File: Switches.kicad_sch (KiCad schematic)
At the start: 29 parts

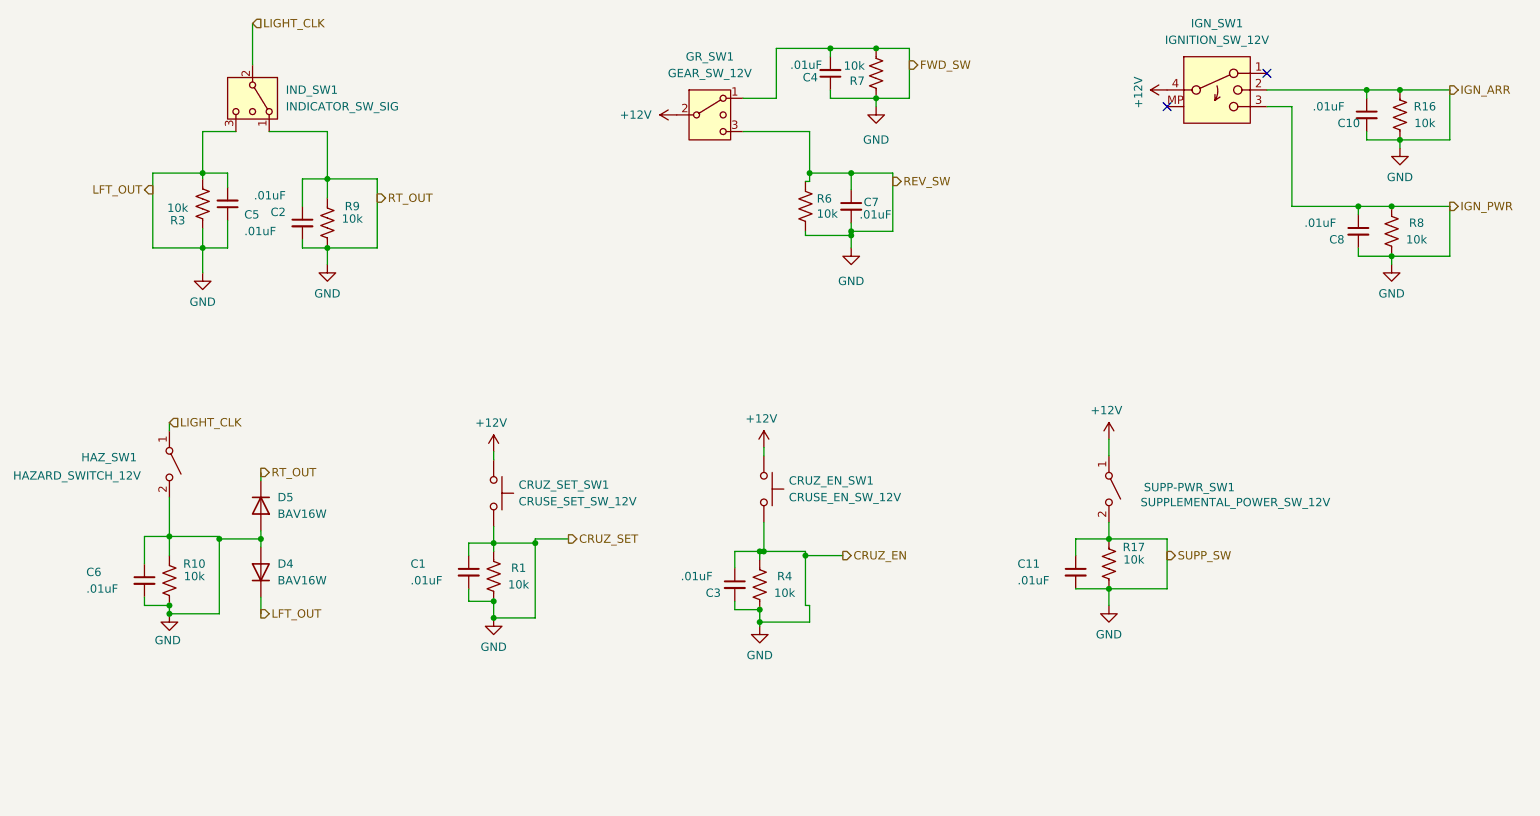
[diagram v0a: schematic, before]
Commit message: Update 1/2
Fixed some of the requested changes.
Still need to fix it up a bit more.
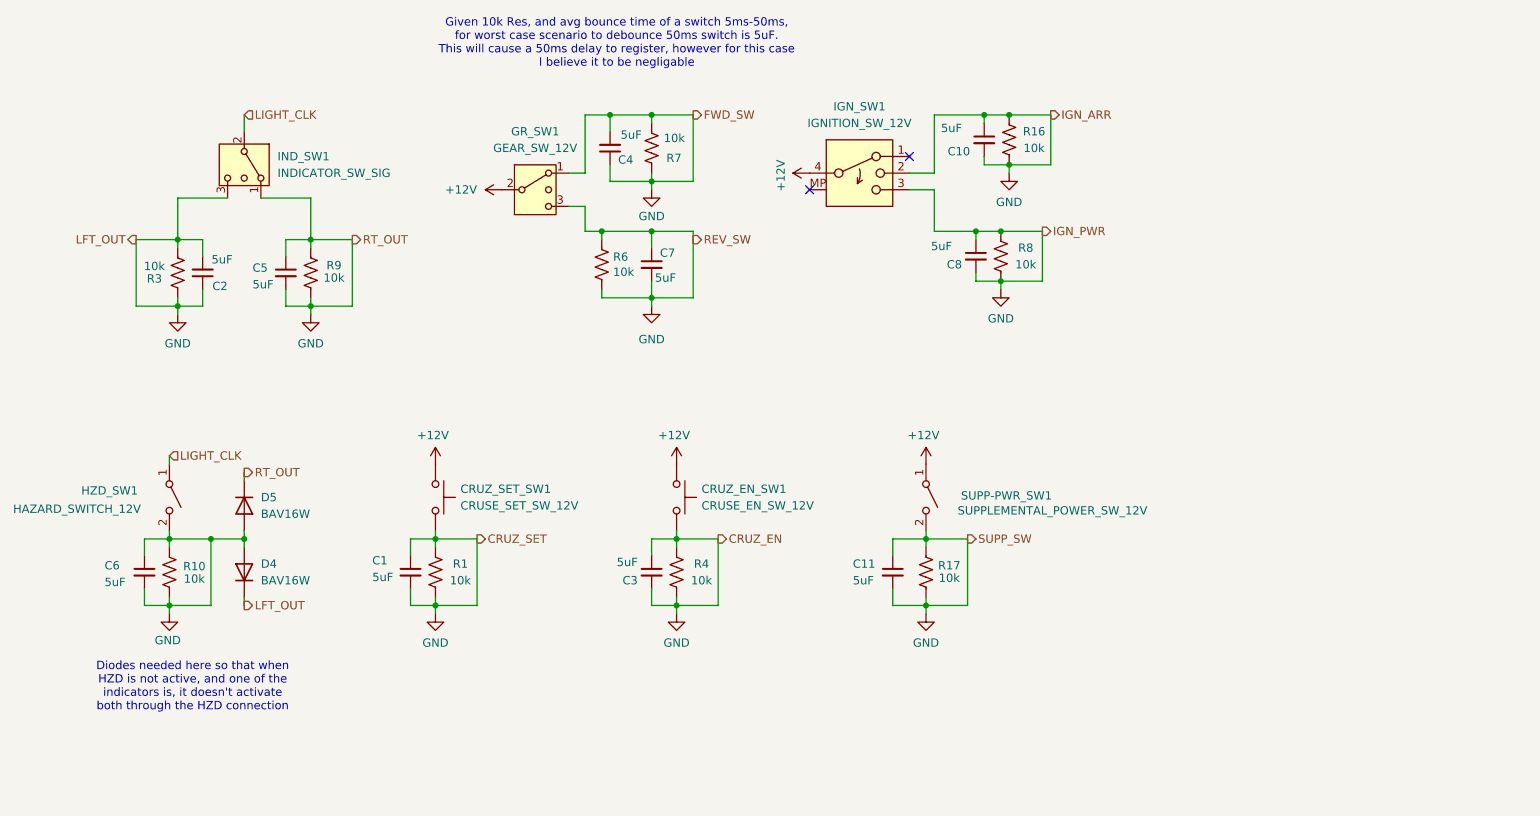
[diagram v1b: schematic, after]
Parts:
- C1, C10, C11, C2, C3, C4, C5, C6, C7, C8: value .01uF -> 5uF
- renumbered HAZ_SW1 to HZD_SW1
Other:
- note added: "Diodes needed here so that when HZD is not active, and one of the indicators is, it doesn't activate both through the HZD connection"
- note added: "Given 10k Res, and avg bounce time of a switch 5ms-50ms, for worst case scenario to debounce 50ms switch is 5uF. This will cause a 50ms delay to register, however for this case I believe it to be negligable"
- moved on the sheet: C1, C10, C11, C2, C3, C4, C5, C6, C7, C8, CRUZ_EN_SW1, CRUZ_SET_SW1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

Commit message: Ready for review
Controls decided to move a bunch of stuff back to leaderboard, also I think I fixed everything else.
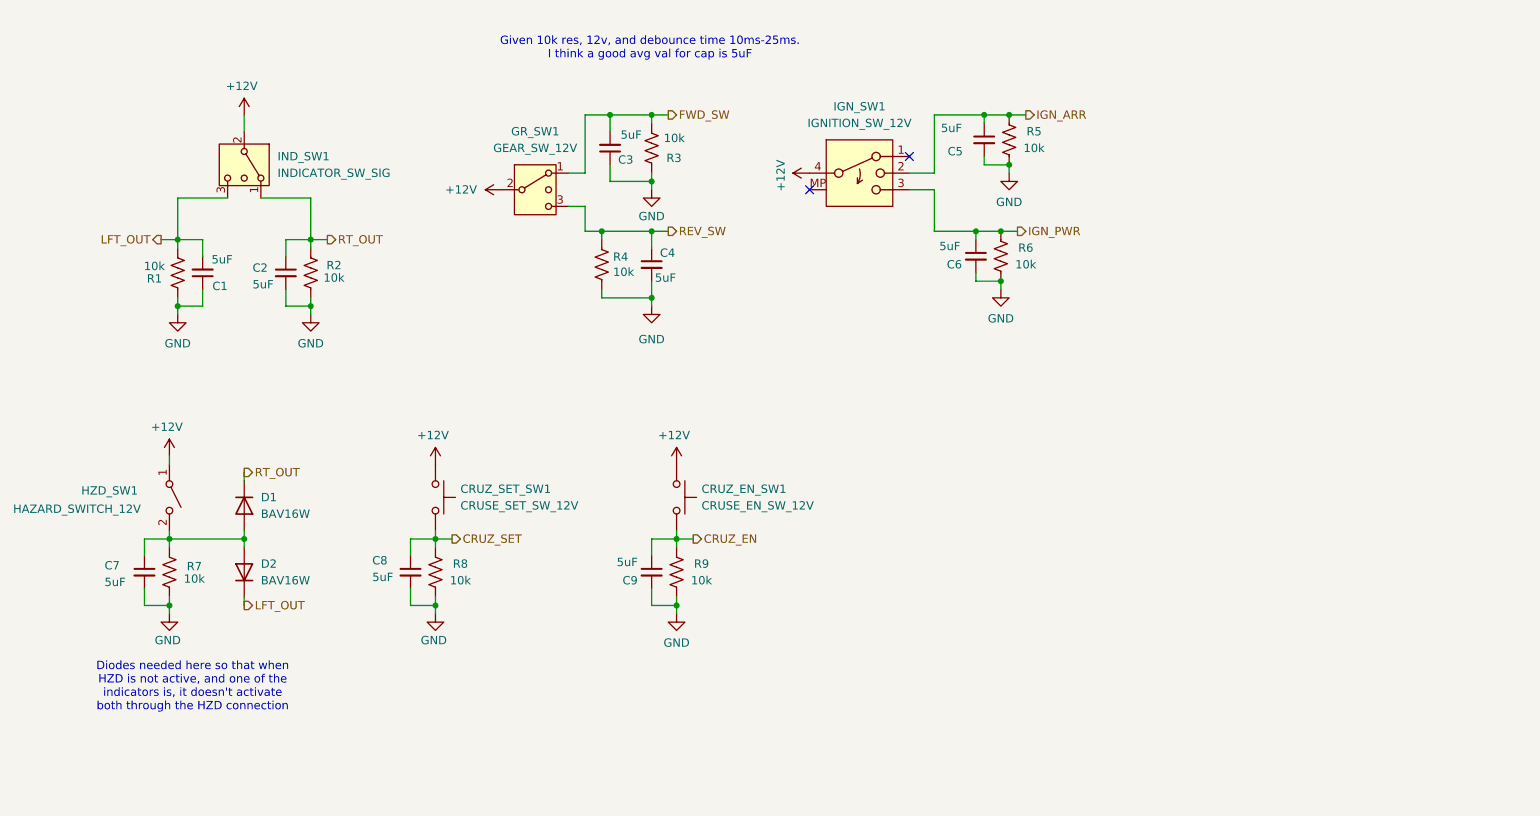
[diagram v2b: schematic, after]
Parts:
- removed C11: 5uF, Capacitor_SMD:C_0805_2012Metric, symbol Device:C_Small
- removed R17: 10k, Resistor_SMD:R_0805_2012Metric, symbol Device:R_US
- removed SUPP-PWR_SW1: SUPPLEMENTAL_POWER_SW_12V, symbol Switch:SW_SPST
- renumbered C2 to C1, C5 to C2, C4 to C3, C7 to C4, C10 to C5, C8 to C6, C6 to C7, C1 to C8, C3 to C9, D5 to D1, D4 to D2, R3 to R1, R9 to R2, R7 to R3, R6 to R4, R16 to R5, R8 to R6, R10 to R7, R1 to R8, R4 to R9
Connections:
- net LIGHT_CLK is gone; now on net +12V: HZD_SW1.1 (A), IND_SW1.2 (3)
- net GND: no longer C1.2, C2.1, C3.2, C4.1, C5.1, C6.1, C7.1, C8.1, C9.1, CRUZ_EN_SW1.2, CRUZ_SET_SW1.2, D1.1 (K), D1.2 (A), D2.1 (K), D2.2 (A), GR_SW1.1, GR_SW1.3 (4), HZD_SW1.2 (B), IGN_SW1.2, IGN_SW1.3, IND_SW1.1, IND_SW1.3 (4), R1.1, R2.2, R3.2, R4.1, R5.2, R6.2, R7.2, R8.1, R9.2
- new net: C7.1, D1.2 (A), D2.2 (A), HZD_SW1.2 (B), R7.2
- new net CRUZ_EN: C9.1, CRUZ_EN_SW1.2, R9.2
- new net CRUZ_SET: C8.1, CRUZ_SET_SW1.2, R8.1
- new net FWD_SW: C3.2, GR_SW1.1, R3.2
- new net IGN_ARR: C5.1, IGN_SW1.2, R5.2
- new net IGN_PWR: C6.1, IGN_SW1.3, R6.2
- new net LFT_OUT: C1.2, D2.1 (K), IND_SW1.3 (4), R1.1
- new net REV_SW: C4.1, GR_SW1.3 (4), R4.1
- new net RT_OUT: C2.1, D1.1 (K), IND_SW1.1, R2.2
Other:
- note added: "Given 10k res, 12v, and debounce time 10ms-25ms. I think a good avg val for cap is 5uF"
- note removed: "Given 10k Res, and avg bounce time of a switch 5ms-50ms, for worst case scenario to debounce 50ms switch is 5uF. This will cause a 50ms delay to register, however for this case I believe it to be negligable"

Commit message: Made pretty
Fixed a few things up and made it pretty.
Still need to double check a few things and assign all footprints
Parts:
- GR_SW1: symbol Switch:SW_SPDT_MSM -> Switch:SW_SP3T
- IGN_SW1: symbol Switch:SW_Rotary_1x3_MP -> Switch:SW_SP3T
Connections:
- net +12V: now also GR_SW1.3, IGN_SW1.3; no longer GR_SW1.2 (3), IGN_SW1.4
- net IGN_PWR: now also IGN_SW1.4; no longer IGN_SW1.3
- net REV_SW: now also GR_SW1.4; no longer GR_SW1.3 (4)
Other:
- note added: "Caps need to be tested to make sure no bouncey"
- note added: "Cruse Buttons"
- note added: "Indicator Switches"
- note added: "Main switches"
- note added: "Nuetral"
- note removed: "Given 10k res, 12v, and debounce time 10ms-25ms. I think a good avg val for cap is 5uF"
- moved on the sheet: C3, C4, C5, C6, C7, C8, C9, CRUZ_EN_SW1, CRUZ_SET_SW1, D1, D2, HZD_SW1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

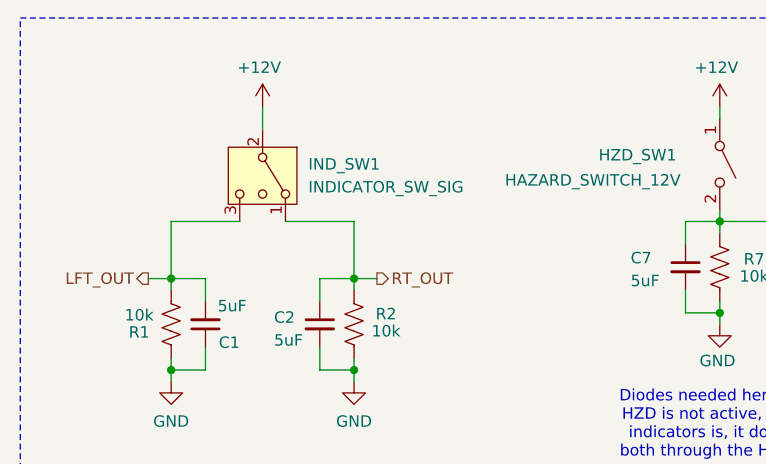
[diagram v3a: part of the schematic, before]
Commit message: Started assigning footprints
Still have a few missing, and not sure if im doing it all right
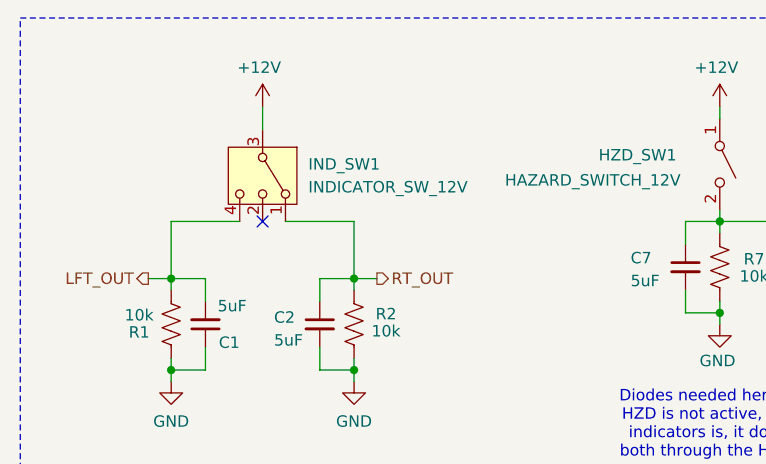
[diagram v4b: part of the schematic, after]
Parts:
- GR_SW1: footprint (none) -> UTSVT_Special:SW_100SP3T1B1M2QEH
- HZD_SW1: footprint (none) -> UTSVT_Special:SW_100SP1T1B4M2QE
- IND_SW1: value INDICATOR_SW_SIG -> INDICATOR_SW_12V; footprint (none) -> UTSVT_Special:SW_100SP3T1B1M2QEH; symbol Switch:SW_SPDT_MSM -> Switch:SW_SP3T
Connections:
- net +12V: now also IND_SW1.3; no longer IND_SW1.2 (3)
- net LFT_OUT: now also IND_SW1.4; no longer IND_SW1.3 (4)
- no-connect marks 2 -> 3
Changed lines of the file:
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@@
+	)
+	(no_connect
+		(at 58.42 52.07)
 	)
 	(no_connect
@@
 			)
 		)
-		(property "Footprint" ""
+		(property "Footprint" "UTSVT_Special:SW_100SP1T1B4M2QE"
 			(at 109.22 45.72 0)
 			(effects
@@
 			)
 		)
-		(property "Datasheet" "~"
+		(property "Datasheet" "https://www.digikey.com/en/products/detail/switch-components/TE1-1A-DC-1-AL/11493057"
 			(at 109.22 45.72 0)
 			(effects
@@
 	)
 	(symbol
-		(lib_id "Switch:SW_SPDT_MSM")
+		(lib_id "Switch:SW_SP3T")
 		(at 58.42 46.99 270)
 		(unit 1)
@@
 			)
 		)
-		(property "Value" "INDICATOR_SW_SIG"
+		(property "Value" "INDICATOR_SW_12V"
 			(at 63.5 48.2599 90)
 			(effects
@@
 			)
 		)
-		(property "Footprint" ""
-			(at 69.85 33.02 0)
+		(property "Footprint" "UTSVT_Special:SW_100SP3T1B1M2QEH"
+			(at 62.865 31.115 0)
 			(effects
 				(font
@@
 			)
 		)
-		(property "Description" "Switch, single pole double throw, center OFF position"
+		(property "Description" "Switch, three position, single pole triple throw, 3 position switch, SP3T"
 			(at 58.42 46.99 0)
 			(effects
@@
 		)
 		(pin "1"
+		)
+		(pin "4"
 		)
 		(instances
@@
 			)
 		)
-		(property "Footprint" ""
+		(property "Footprint" "UTSVT_Special:SW_100SP3T1B1M2QEH"
 			(at 153.035 45.085 0)
 			(effects

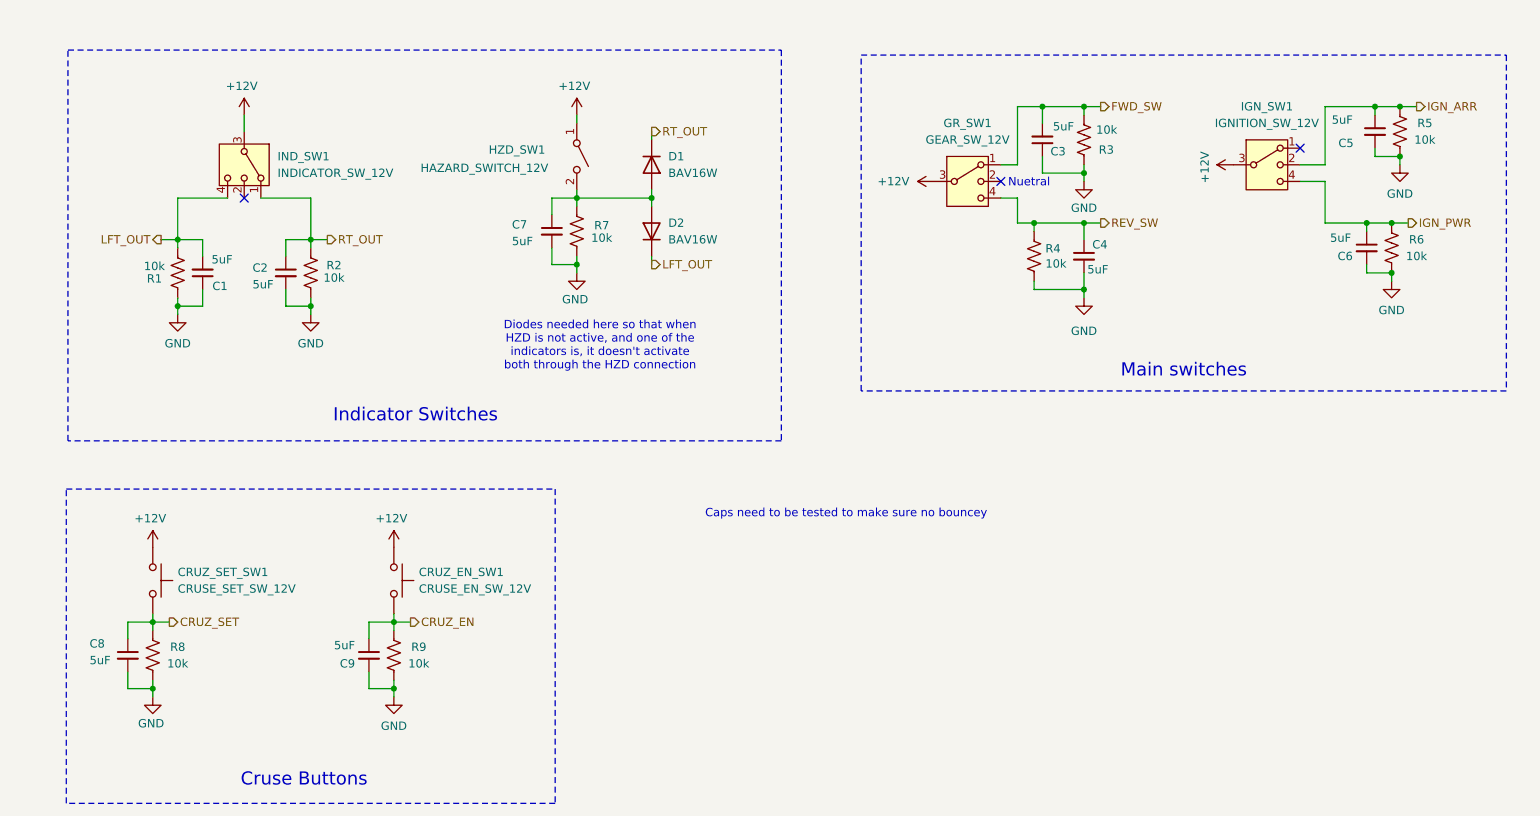
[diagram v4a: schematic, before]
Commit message: Added a lot footprints
Some of them are custom and need to be double checked. Also no sure if they are all correctly included
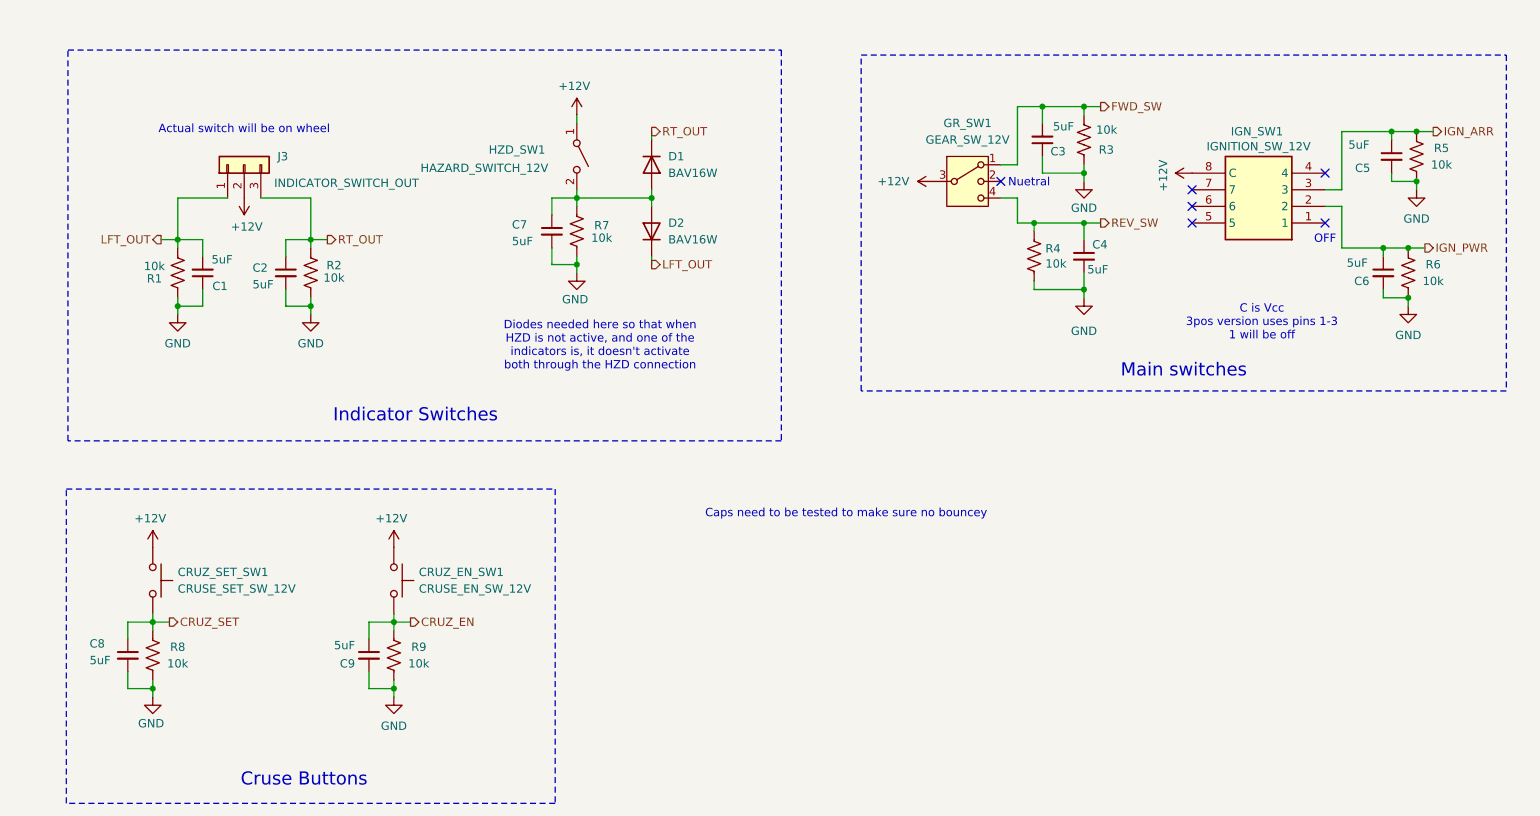
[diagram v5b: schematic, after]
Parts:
- removed IND_SW1: INDICATOR_SW_12V, UTSVT_Special:SW_100SP3T1B1M2QEH, symbol Switch:SW_SP3T
- added J3: INDICATOR_SWITCH_OUT, Connector_Molex:Molex_Micro-Fit_3.0_43650-0300_1x03_P3.00mm_Horizontal, symbol Connector_Generic:Conn_01x03
- CRUZ_EN_SW1, CRUZ_SET_SW1: footprint (none) -> UTSVT_Special:SW_Butt_)
- GR_SW1: footprint UTSVT_Special:SW_100SP3T1B1M2QEH -> UTSVT_Special:SW_100_SP3T-Vertical
- HZD_SW1: footprint UTSVT_Special:SW_100SP1T1B4M2QE -> UTSVT_Special:SW_HAZARD
- IGN_SW1: footprint (none) -> switched:RM103772BCB; symbol Switch:SW_SP3T -> RM103772BCB:RM103772BCB; Height (none) -> 15.1; Manufacturer_Name (none) -> C & K COMPONENTS; Manufacturer_Part_Number (none) -> RM103772BCB; Mouser Part Number (none) -> 611-RM103772BCB; Mouser Price/Stock (none) -> https://www.mouser.co.uk/ProductDetail/CK/RM103772BCB?qs=36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
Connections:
- net +12V: now also IGN_SW1.8 (C), J3.2 (Pin_2); no longer IGN_SW1.3
- net IGN_ARR: now also IGN_SW1.3; no longer IGN_SW1.2
- net IGN_PWR: now also IGN_SW1.2; no longer IGN_SW1.4
- net LFT_OUT: now also J3.1 (Pin_1)
- net RT_OUT: now also J3.3 (Pin_3)
- no-connect marks 3 -> 6
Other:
- note added: "Actual switch will be on wheel"
- note added: "C is Vcc 3pos version uses pins 1-3 1 will be off"
- note added: "OFF"
- moved on the sheet: C5, C6, R5, R6

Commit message: Added footprints locally
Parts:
- CRUZ_EN_SW1, CRUZ_SET_SW1: footprint UTSVT_Special:SW_Butt_) -> switched:SW_Butt_)
- GR_SW1: footprint UTSVT_Special:SW_100_SP3T-Vertical -> switched:SW_100_SP3T-Vertical
- HZD_SW1: footprint UTSVT_Special:SW_HAZARD -> switched:SW_HAZARD
- IGN_SW1: footprint switched:RM103772BCB -> switched:SW_ROT_3POS
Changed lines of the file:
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@@
 			)
 		)
-		(property "Footprint" "UTSVT_Special:SW_HAZARD"
+		(property "Footprint" "switched:SW_HAZARD"
 			(at 109.22 45.72 0)
 			(effects
@@
 			)
 		)
-		(property "Footprint" "UTSVT_Special:SW_100_SP3T-Vertical"
+		(property "Footprint" "switched:SW_100_SP3T-Vertical"
 			(at 153.035 45.085 0)
 			(effects
@@
 			)
 		)
-		(property "Footprint" "switched:RM103772BCB"
+		(property "Footprint" "switched:SW_ROT_3POS"
 			(at 207.01 -39.04 0)
 			(effects
@@
 			)
 		)
-		(property "Footprint" "UTSVT_Special:SW_Butt_)"
+		(property "Footprint" "switched:SW_Butt_)"
 			(at 49.53 110.49 0)
 			(effects
@@
 			)
 		)
-		(property "Footprint" "UTSVT_Special:SW_Butt_)"
+		(property "Footprint" "switched:SW_Butt_)"
 			(at 86.36 110.49 0)
 			(effects
